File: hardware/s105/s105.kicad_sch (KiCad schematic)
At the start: 50 parts, among them P1 368255-2

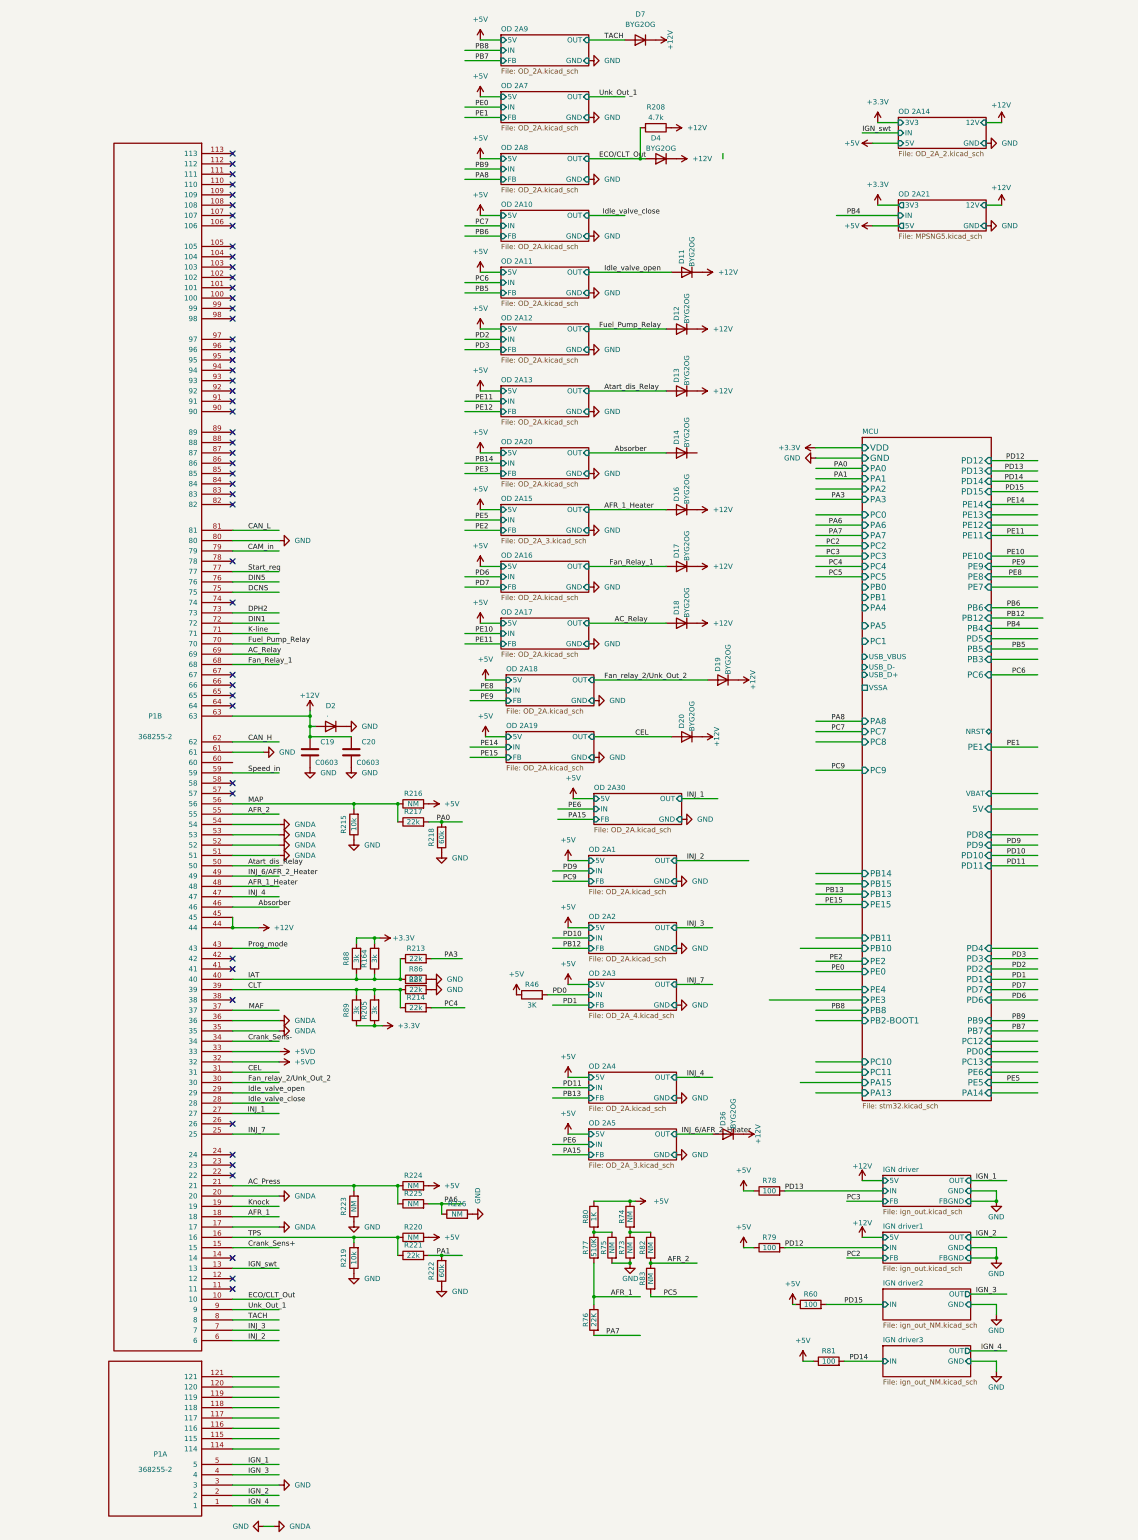
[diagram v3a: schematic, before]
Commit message: новые модули, продолжение расположения
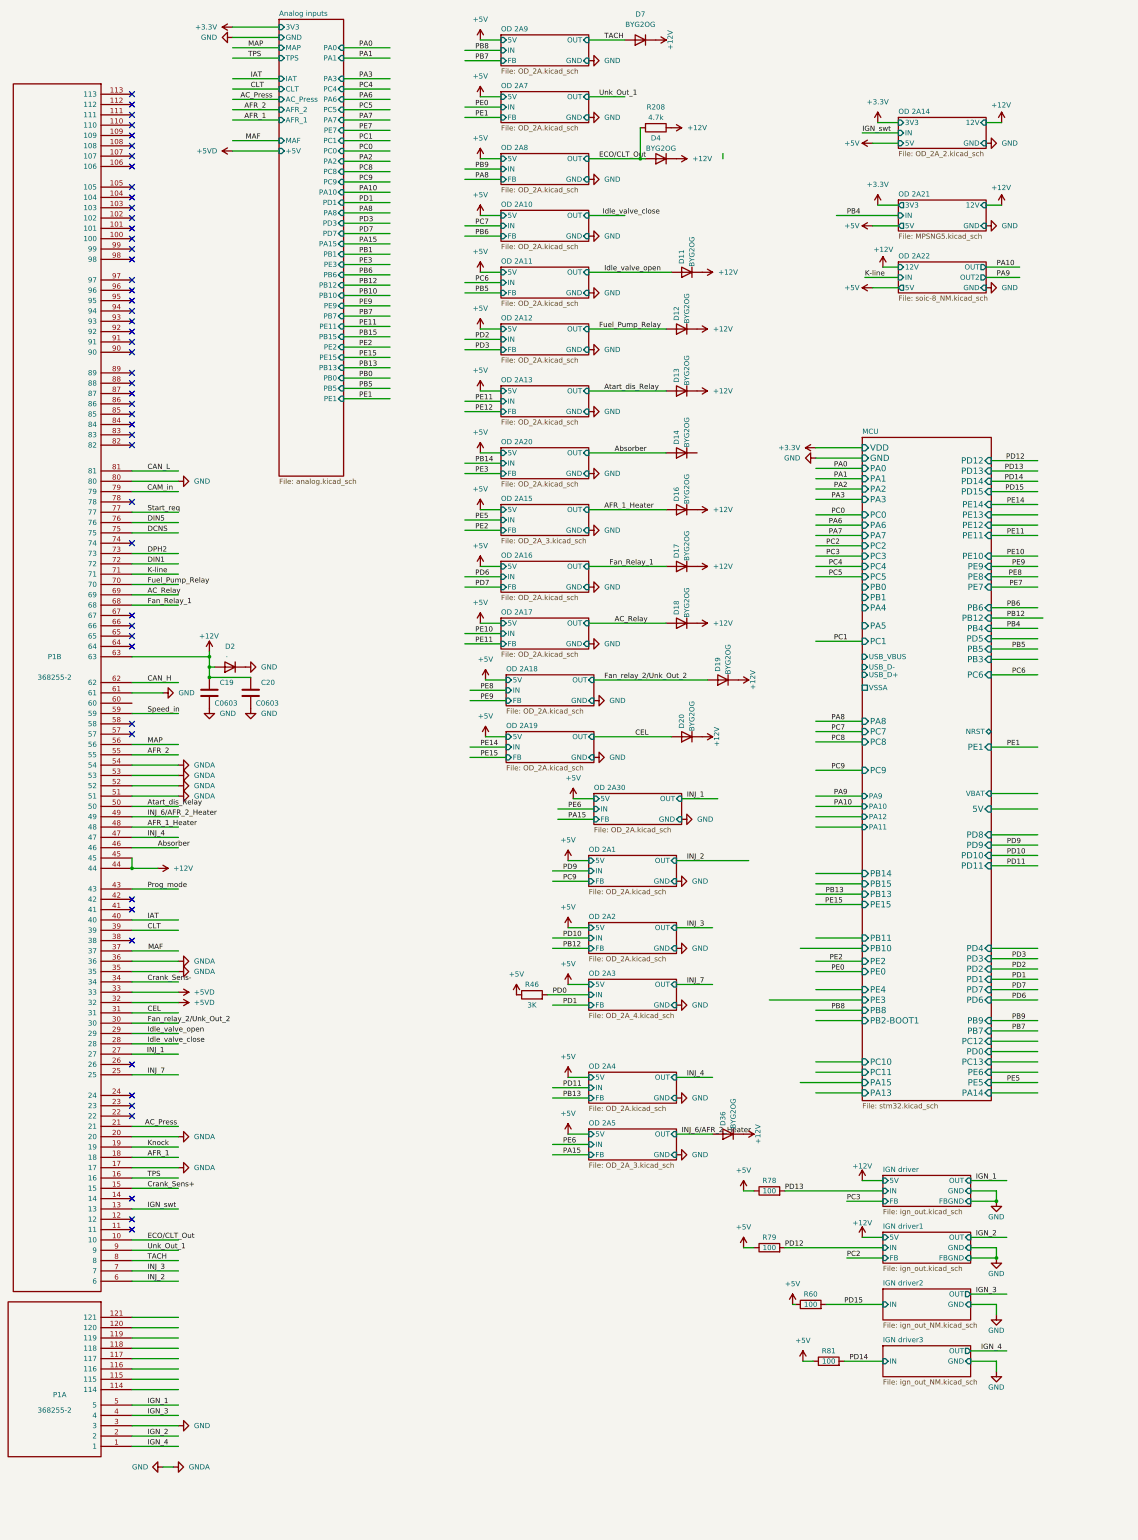
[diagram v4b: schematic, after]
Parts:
- removed R164, R205, R88, R89: 3k, Resistor_SMD:R_1206_3216Metric, symbol Device:R
- removed R213, R214, R217, R221, R86, R87: 22k, Resistor_SMD:R_0603_1608Metric, symbol Device:R
- removed R215, R219: 10k, Resistor_SMD:R_0603_1608Metric, symbol Device:R
- removed R216, R220, R223, R224, R225, R226, R73, R74, R75, R82, R83: NM, Resistor_SMD:R_0603_1608Metric, symbol Device:R
- removed R218, R222: 60k, Resistor_SMD:R_0603_1608Metric, symbol Device:R
- removed R76: 22K, Resistor_SMD:R_0603_1608Metric, symbol Device:R
- removed R77: 510K, Resistor_SMD:R_0603_1608Metric, symbol Device:R
- removed R80: 1K, Resistor_SMD:R_0603_1608Metric, symbol Device:R
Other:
- added sheet Analog inputs (analog.kicad_sch)
- added sheet OD 2A22 (soic-8_NM.kicad_sch)
- sheet MCU ports: added PA10, PA11, PA12, PA9; removed none
- moved on the sheet: C19, C20, D2, P1A, P1B

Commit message: заполняем плату дальше
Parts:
- added C48, C49, C55, C71, C73, C78, C80, C81, C82, C83, C84, C85, C87, C88: C0603, Capacitor_SMD:C_0603_1608Metric, symbol Device:C
- added C79: 100nF, Capacitor_SMD:C_0603_1608Metric, symbol Device:C
- added R256, R257, R258, R259, R260: 0, Resistor_SMD:R_0805_2012Metric, symbol Device:R
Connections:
- net +5VD: now also C87.1
- net CAM_in: now also C88.1
- net CAN_H: now also C84.1
- net CAN_L: now also C85.1
- net DCNS: now also C73.1
- net DIN1: now also C80.1
- net DIN5: now also C83.1
- net DPH2: now also C81.1
- net GND: now also C48.2, C49.2, C55.2, C71.2, C73.2, C78.2, C79.1, C80.2, C81.2, C82.2, C83.2, C84.2, C85.2, C87.2, C88.2, R256.2, R257.2, R258.2, R259.2, R260.2; no longer P1.17, P1.20, P1.35, P1.36, P1.51, P1.52, P1.53, P1.54
- net IGN_swt: now also C49.1
- net Knock: now also C71.1
- net Prog_mode: now also C79.2
- net Speed_in: now also C78.1
- net Start_req: now also C82.1
- net at P1.12: now also C48.1
- net at P1.14: now also C55.1
- new net GNDA: P1.17, P1.20, P1.35, P1.36, P1.51, P1.52, P1.53, P1.54, R256.1, R257.1, R258.1, R259.1, R260.1
- no-connect marks 50 -> 48
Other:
- added sheet OD 2A23 (ak1sl.kicad_sch)
- added sheet OD 2A24 (ak1sl2.kicad_sch)

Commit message: +knock
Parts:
- removed C71: C0603, Capacitor_SMD:C_0603_1608Metric, symbol Device:C
- R60, R78, R79, R81: value 100 -> 10
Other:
- removed sheet OD 2A23
- added sheet LM A1 (LM2902.kicad_sch)
- added sheet VR A1 (VR.kicad_sch)

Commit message: can, analog inputs
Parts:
- removed C48, C73, C78, C84, C85, C88: C0603, Capacitor_SMD:C_0603_1608Metric, symbol Device:C
- removed C79: 100nF, Capacitor_SMD:C_0603_1608Metric, symbol Device:C
- D11, D12, D13, D14, D16, D17, D18, D19, D20, D36, D4, D7: value BYG2OG -> .
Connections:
- net NEW_PIN: now reaches P1.12
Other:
- added sheet CAN A1 (CAN.kicad_sch)
- sheet Analog inputs ports: added 12V, BOOT0, CAM_in, DCNS, NEW_PIN, PB11, PB3, PC13, PD5, Prog_mode, Speed_in, VBAT; removed none
- sheet MCU ports: added BOOT0; removed none
- moved on the sheet: D11, D12, D13, D14, D16, D17, D18, D19, D20, D36, D4, D7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

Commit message: закончила пока что
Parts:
- removed C49, C80, C81, C82, C83, C87: C0603, Capacitor_SMD:C_0603_1608Metric, symbol Device:C
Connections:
- net +12V: now also D14.1 (K)
- no-connect marks 48 -> 57
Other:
- sheet CAN A1 renamed CAN
- sheet LM A1 renamed Knock
- added sheet Power 12 to 3.3 (MA84795A.kicad_sch)
- added sheet Power 5V (MA84795A2.kicad_sch)
- sheet Analog inputs ports: added +3.3V, DIN1, DIN5, DPH2, PC10, PC11, PC12, PD4, Start_req; removed 3V3, PA2
- sheet Knock ports: added OUT2; removed none
- sheet MCU ports: added none; removed 5V, NRST, USB_D+, USB_D-, USB_VBUS
- sheet OD 2A14 ports: added OUT; removed IN
- sheet OD 2A21 ports: added none; removed 3V3
- sheet OD 2A22 ports: added 3V3; removed none
- sheet OD 2A24 ports: added IN; removed none
- sheet OD 2A3 ports: added none; removed 5V
- sheet OD 2A5 ports: added OUT2; removed none
- note added: "???????????"
- moved on the sheet: C55, R46
